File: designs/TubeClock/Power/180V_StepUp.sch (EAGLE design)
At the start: 16 parts, among them IC1 MAX1771, Q1 RF644

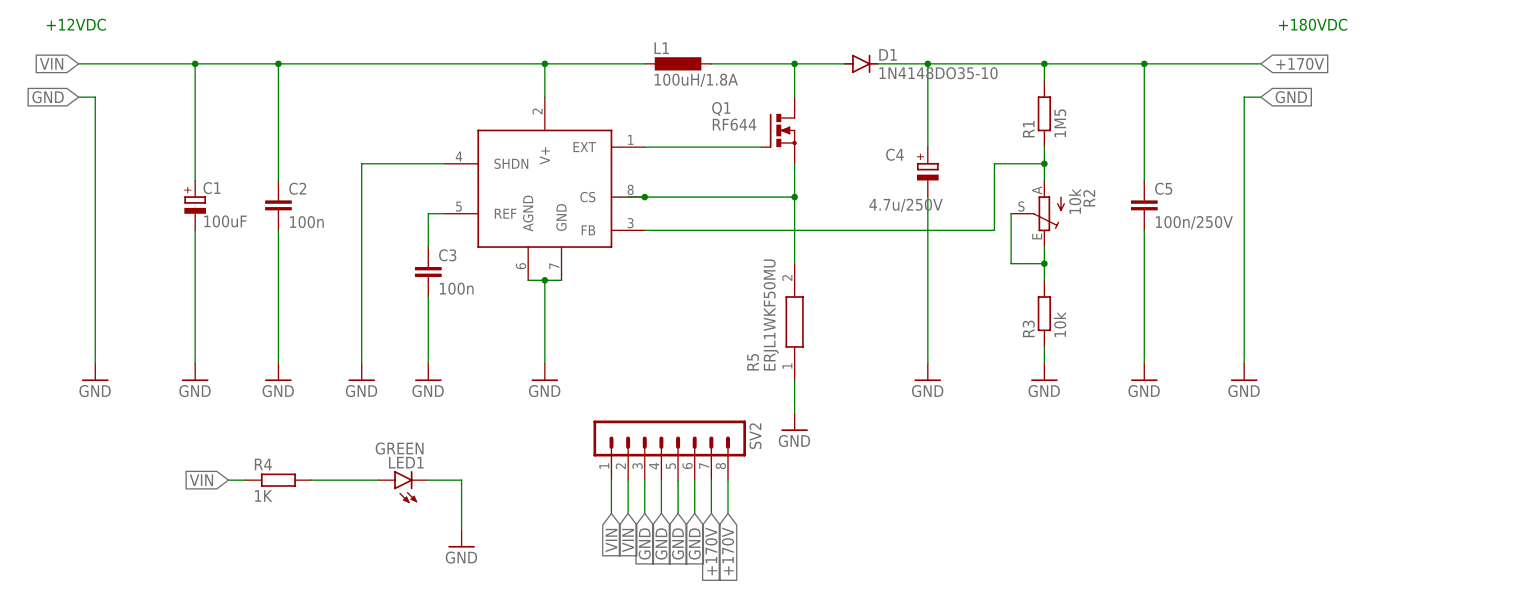
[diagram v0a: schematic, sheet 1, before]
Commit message: small changes to easter radio mainboard started for in14 nixi tubes and cleanup
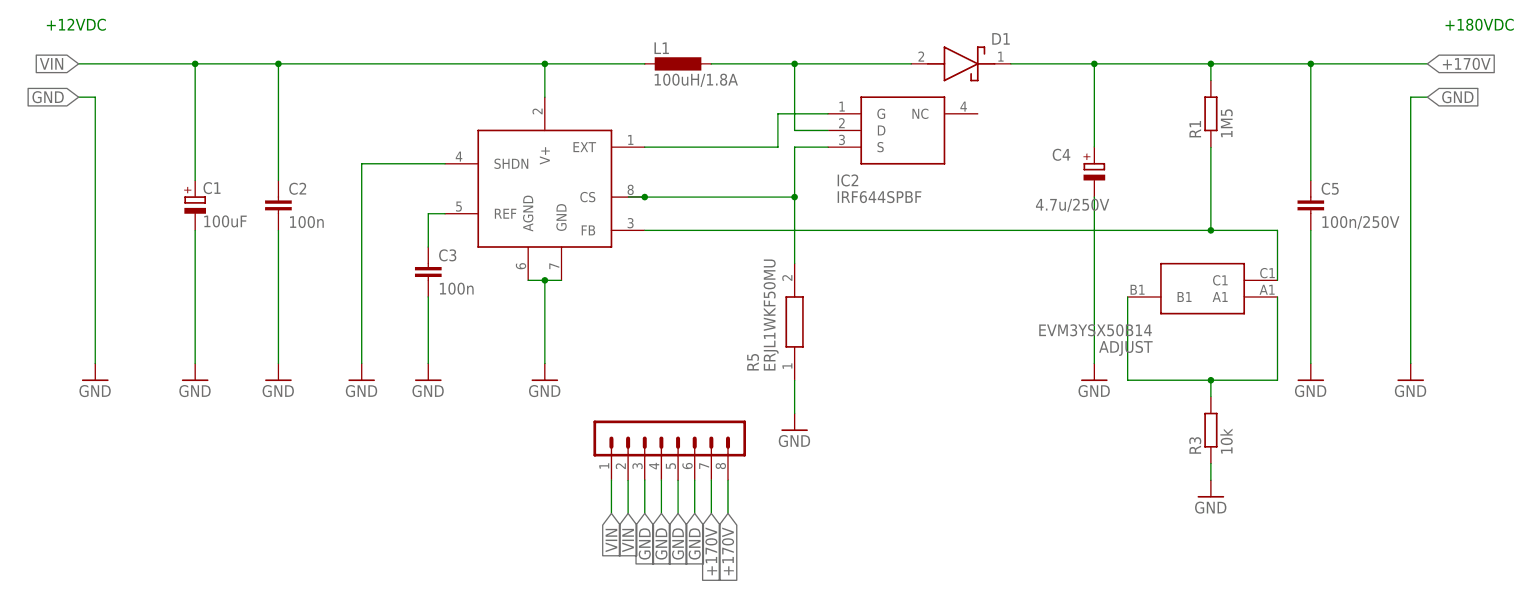
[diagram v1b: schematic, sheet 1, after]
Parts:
- removed LED1: GREEN, CommonParts:LED_1206SMT1206
- removed Q1: RF644, transistor-power:PMOSFET_NTO220BV
- removed R2: 10k, pot:TRIM_EU-RJ9W
- removed R4: 1K, CommonParts:R-EU_1206R1206
- removed SV2: (no value), con-lstb:MA08-1
- added ADJUST: EVM3YSX50B14, CommonParts:EVM3YSX50B14
- added IC2: IRF644SPBF, MouserUseful:IRF644SPBF
- added SV1: (no value), CommonParts:PINHEADER-1X8
- D1: value 1N4148DO35-10 -> LSM115JE3_TR13; device diode:1N4148DO35-10 -> CommonParts:LSM115JE3_TR13
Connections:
- removed net N$1: LED1.A, R4.2
- net +170V: now also D1.K, SV1.7, SV1.8; no longer D1.C, SV2.7, SV2.8
- net GND: now also SV1.3, SV1.4, SV1.5, SV1.6; no longer LED1.C, SV2.3, SV2.4, SV2.5, SV2.6
- net N$2: now also IC2.D; no longer Q1.D
- net N$4: now also IC2.G; no longer Q1.G
- net N$5: now also IC2.S; no longer Q1.S
- net N$6: now also ADJUST.C1; no longer R2.A
- net N$7: now also ADJUST.A1, ADJUST.B1; no longer R2.E, R2.S
- net VIN: now also SV1.1, SV1.2; no longer R4.1, SV2.1, SV2.2
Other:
- moved on the sheet: C4, C5, R1, R3
